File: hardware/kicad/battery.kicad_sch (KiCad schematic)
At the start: 4 parts, among them J2 +LIPO, J3 -LIPO, Q1 AO3407A

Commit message: clean-up
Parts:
- TP1: footprint TestPoint:TestPoint_Pad_D1.5mm -> TestPoint:TestPoint_Pad_D1.0mm
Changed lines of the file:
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@@
       (effects (font (size 1.27 1.27)))
     )
-    (property "Footprint" "TestPoint:TestPoint_Pad_D1.5mm" (at 111.76 52.07 0)
+    (property "Footprint" "TestPoint:TestPoint_Pad_D1.0mm" (at 111.76 52.07 0)
       (effects (font (size 1.27 1.27)) hide)
     )
@@
       (effects (font (size 1.27 1.27)) hide)
     )
+    (property "Part Description" "" (at 106.68 52.07 0)
+      (effects (font (size 1.27 1.27)) hide)
+    )
+    (property "Manufacturer" "" (at 106.68 52.07 0)
+      (effects (font (size 1.27 1.27)) hide)
+    )
+    (property "Manufacturer Part Number" "" (at 106.68 52.07 0)
+      (effects (font (size 1.27 1.27)) hide)
+    )
+    (property "Distributor" "" (at 106.68 52.07 0)
+      (effects (font (size 1.27 1.27)) hide)
+    )
+    (property "Distributor Part Number" "" (at 106.68 52.07 0)
+      (effects (font (size 1.27 1.27)) hide)
+    )
+    (property "Distributor Link" "" (at 106.68 52.07 0)
+      (effects (font (size 1.27 1.27)) hide)
+    )

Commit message: change batt footprint
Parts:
- J3: footprint TestPoint:TestPoint_Pad_2.0x2.0mm -> TestPoint:TestPoint_Loop_D1.80mm_Drill1.0mm_Beaded
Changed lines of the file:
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@@
       (effects (font (size 1.27 1.27)))
     )
-    (property "Footprint" "TestPoint:TestPoint_Pad_2.0x2.0mm" (at 101.6 64.77 0)
+    (property "Footprint" "TestPoint:TestPoint_Loop_D1.80mm_Drill1.0mm_Beaded" (at 101.6 64.77 0)
       (effects (font (size 1.27 1.27)) hide)
     )
@@
       (effects (font (size 1.27 1.27)) hide)
     )
+    (property "Manufacturer" "" (at 101.6 64.77 0)
+      (effects (font (size 1.27 1.27)) hide)
+    )
+    (property "Manufacturer Part Number" "" (at 101.6 64.77 0)
+      (effects (font (size 1.27 1.27)) hide)
+    )
+    (property "Distributor" "" (at 101.6 64.77 0)
+      (effects (font (size 1.27 1.27)) hide)
+    )
+    (property "Distributor Part Number" "" (at 101.6 64.77 0)
+      (effects (font (size 1.27 1.27)) hide)
+    )
+    (property "Distributor Link" "" (at 101.6 64.77 0)
+      (effects (font (size 1.27 1.27)) hide)
+    )

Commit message: change batt footprint
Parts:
- J2: footprint TestPoint:TestPoint_Pad_2.0x2.0mm -> TestPoint:TestPoint_THTPad_D1.0mm_Drill0.5mm
- J3: footprint TestPoint:TestPoint_Loop_D1.80mm_Drill1.0mm_Beaded -> TestPoint:TestPoint_THTPad_D1.0mm_Drill0.5mm
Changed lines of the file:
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@@
       (effects (font (size 1.27 1.27)))
     )
-    (property "Footprint" "TestPoint:TestPoint_Pad_2.0x2.0mm" (at 101.6 59.69 0)
+    (property "Footprint" "TestPoint:TestPoint_THTPad_D1.0mm_Drill0.5mm" (at 101.6 59.69 0)
       (effects (font (size 1.27 1.27)) hide)
     )
@@
     )
     (property "Part Description" "On-board Pad" (at 101.6 59.69 0)
+      (effects (font (size 1.27 1.27)) hide)
+    )
+    (property "Manufacturer" "" (at 101.6 59.69 0)
+      (effects (font (size 1.27 1.27)) hide)
+    )
+    (property "Manufacturer Part Number" "" (at 101.6 59.69 0)
+      (effects (font (size 1.27 1.27)) hide)
+    )
+    (property "Distributor" "" (at 101.6 59.69 0)
+      (effects (font (size 1.27 1.27)) hide)
+    )
+    (property "Distributor Part Number" "" (at 101.6 59.69 0)
+      (effects (font (size 1.27 1.27)) hide)
+    )
+    (property "Distributor Link" "" (at 101.6 59.69 0)
       (effects (font (size 1.27 1.27)) hide)
     )
@@
       (effects (font (size 1.27 1.27)))
     )
-    (property "Footprint" "TestPoint:TestPoint_Loop_D1.80mm_Drill1.0mm_Beaded" (at 101.6 64.77 0)
+    (property "Footprint" "TestPoint:TestPoint_THTPad_D1.0mm_Drill0.5mm" (at 101.6 64.77 0)
       (effects (font (size 1.27 1.27)) hide)
     )

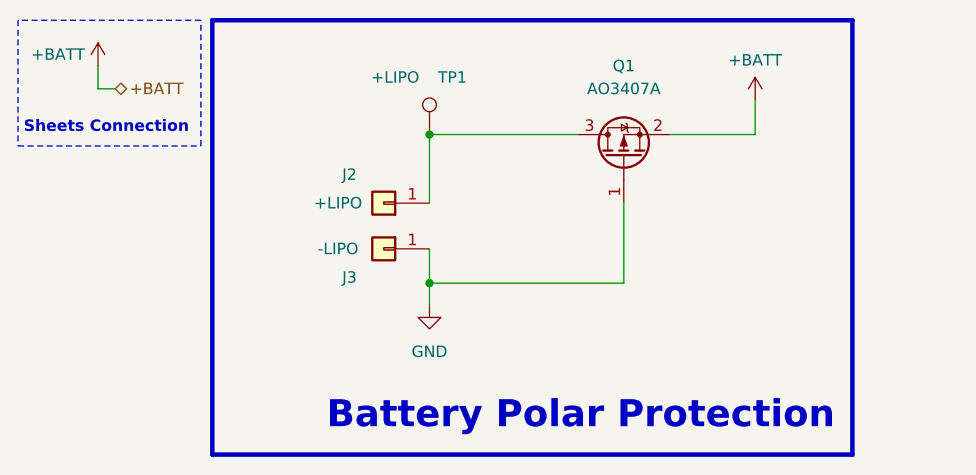
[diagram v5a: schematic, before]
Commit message: add jst battery
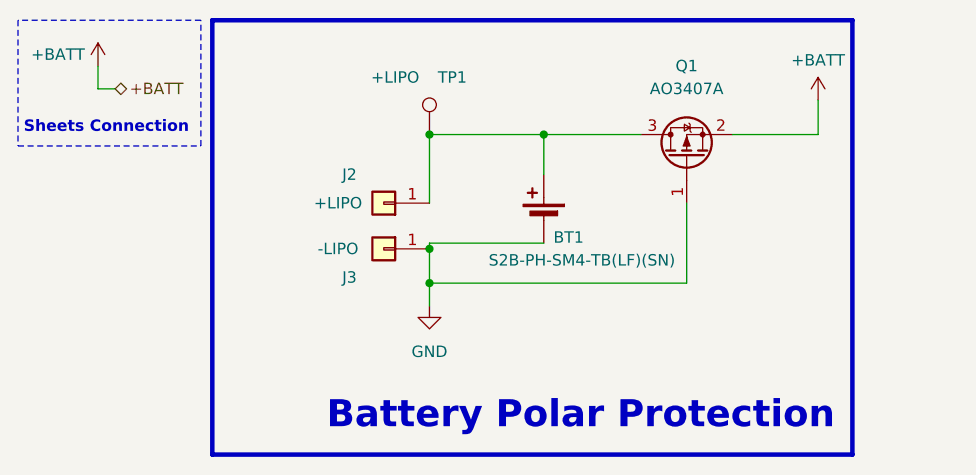
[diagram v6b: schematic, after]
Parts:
- added BT1: S2B-PH-SM4-TB(LF)(SN), plantpal:JST_PH_S2B-PH-SM4-TB_1x02-1MP_P2.00mm_Horizontal, symbol Device:Battery_Cell
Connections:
- net GND: now also BT1.2 (-)
- net at J2.1 (Pin_1), Q1.3 (D), TP1.1: now also BT1.1 (+)
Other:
- moved on the sheet: Q1
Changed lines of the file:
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@@
   (junction (at 106.68 52.07) (diameter 0) (color 0 0 0 0)
   )
+  (junction (at 119.38 52.07) (diameter 0) (color 0 0 0 0)
+  )
+  (junction (at 106.68 64.77) (diameter 0) (color 0 0 0 0)
+  )
   (junction (at 106.68 68.58) (diameter 0) (color 0 0 0 0)
   )
-  (wire (pts (xy 128.27 59.69) (xy 128.27 68.58))
+  (wire (pts (xy 135.255 59.69) (xy 135.255 68.58))
     (stroke (width 0) (type default))
   )
@@
     (stroke (width 0) (type dash))
   )
-  (wire (pts (xy 142.875 48.26) (xy 142.875 52.07))
+  (wire (pts (xy 106.68 68.58) (xy 106.68 71.12))
+    (stroke (width 0) (type default))
+  )
+  (wire (pts (xy 149.86 48.26) (xy 149.86 52.07))
     (stroke (width 0) (type default))
   )
@@
     (stroke (width 0) (type dash))
   )
+  (wire (pts (xy 119.38 52.07) (xy 130.175 52.07))
+    (stroke (width 0) (type default))
+  )
   (polyline (pts (xy 153.67 39.37) (xy 153.67 87.63))
     (stroke (width 0.5) (type default))
@@
     (stroke (width 0) (type default))
   )
-  (wire (pts (xy 133.35 52.07) (xy 142.875 52.07))
+  (wire (pts (xy 140.335 52.07) (xy 149.86 52.07))
     (stroke (width 0) (type default))
   )
@@
     (stroke (width 0.5) (type default))
   )
+  (wire (pts (xy 119.38 64.135) (xy 106.68 64.135))
+    (stroke (width 0) (type default))
+  )
   (polyline (pts (xy 81.28 53.34) (xy 81.28 39.37))
     (stroke (width 0) (type dash))
   )
-  (wire (pts (xy 106.68 68.58) (xy 106.68 71.12))
-    (stroke (width 0) (type default))
-  )
   (wire (pts (xy 106.68 64.77) (xy 106.68 68.58))
     (stroke (width 0) (type default))
   )
-  (wire (pts (xy 106.68 68.58) (xy 128.27 68.58))
+  (wire (pts (xy 119.38 52.07) (xy 119.38 56.515))
+    (stroke (width 0) (type default))
+  )
+  (wire (pts (xy 106.68 68.58) (xy 135.255 68.58))
     (stroke (width 0) (type default))
   )
@@
     (stroke (width 0.5) (type default))
   )
+  (wire (pts (xy 106.68 64.135) (xy 106.68 64.77))
+    (stroke (width 0) (type default))
+  )
   (wire (pts (xy 69.85 46.99) (xy 71.755 46.99))
     (stroke (width 0) (type default))
@@
     (stroke (width 0.5) (type default))
   )
-  (wire (pts (xy 106.68 52.07) (xy 123.19 52.07))
+  (wire (pts (xy 106.68 52.07) (xy 119.38 52.07))
     (stroke (width 0) (type default))
   )
@@
     (effects (font (size 1.27 1.27)) (justify left))
   )
-  (symbol (lib_id "Device:Q_PMOS_GSD") (at 128.27 54.61 90) (unit 1)
+  (symbol (lib_id "Device:Battery_Cell") (at 119.38 61.595 0) (mirror y) (unit 1)
+    (in_bom yes) (on_board yes) (dnp no)
+    (property "Reference" "BT1" (at 123.825 63.5 0)
+      (effects (font (size 1.27 1.27)) (justify left))
+    )
+    (property "Value" "S2B-PH-SM4-TB(LF)(SN)" (at 133.985 66.04 0)
+      (effects (font (size 1.27 1.27)) (justify left))
+    )
+    (property "Footprint" "plantpal:JST_PH_S2B-PH-SM4-TB_1x02-1MP_P2.00mm_Horizontal" (at 119.38 60.071 90)
+      (effects (font (size 1.27 1.27)) hide)
+    )
+    (property "Datasheet" "https://datasheet.lcsc.com/lcsc/2102031704_JST-Sales-America-S2B-PH-SM4-TB-LF-SN_C295747.pdf" (at 119.38 60.071 90)
+      (effects (font (size 1.27 1.27)) hide)
+    )
+    (property "Part Description" "Wire To Board Connector 1x2P PH 2mm Male 2A P=2mm" (at 119.38 61.595 0)
+      (effects (font (size 1.27 1.27)) hide)
+    )
+    (property "Manufacturer" "JST Sales America" (at 119.38 61.595 0)
+      (effects (font (size 1.27 1.27)) hide)
+    )
+    (property "Manufacturer Part Number" "S2B-PH-SM4-TB(LF)(SN)" (at 119.38 61.595 0)
+      (effects (font (size 1.27 1.27)) hide)
+    )
+    (property "Distributor" "LCSC" (at 119.38 61.595 0)
+      (effects (font (size 1.27 1.27)) hide)
+    )
+    (property "Distributor Part Number" "C295747" (at 119.38 61.595 0)
+      (effects (font (size 1.27 1.27)) hide)
+    )
+    (property "Distributor Link" "https://www.lcsc.com/product-detail/Wire-To-Board-Wire-To-Wire-Connector_JST-Sales-America-S2B-PH-SM4-TB-LF-SN_C295747.html" (at 119.38 61.595 0)
+      (effects (font (size 1.27 1.27)) hide)
+    )
+    (pin "1")
+    (pin "2")
+    (instances
+      (project "plantpal"
+        (path "/59b4123e-c7be-466b-a5db-658b8f0c1171/76cc1a03-b597-4ef0-85b8-85a2d617e76b"
+          (reference "BT1") (unit 1)
+        )
+      )
+    )
+  )
+  (symbol (lib_id "Device:Q_PMOS_GSD") (at 135.255 54.61 90) (unit 1)
     (in_bom yes) (on_board yes) (dnp no) (fields_autoplaced)
-    (property "Reference" "Q1" (at 128.27 44.45 90)
-      (effects (font (size 1.27 1.27)))
-    )
-    (property "Value" "AO3407A" (at 128.27 46.99 90)
-      (effects (font (size 1.27 1.27)))
-    )
-    (property "Footprint" "Package_TO_SOT_SMD:SOT-23" (at 125.73 49.53 0)
-      (effects (font (size 1.27 1.27)) hide)
-    )
-    (property "Datasheet" "https://datasheet.lcsc.com/lcsc/1810231523_Alpha---Omega-Semicon-AO3407A_C15155.pdf" (at 128.27 54.61 0)
-      (effects (font (size 1.27 1.27)) hide)
-    )
-    (property "Part Description" "MOSFET P Channel 30V 4.3A 48mΩ@10V,4.3A 1.4W" (at 128.27 54.61 0)
-      (effects (font (size 1.27 1.27)) hide)
-    )
-    (property "Manufacturer" "Alpha & Omega Semicon" (at 128.27 54.61 0)
-      (effects (font (size 1.27 1.27)) hide)
-    )
-    (property "Manufacturer Part Number" "AO3407A" (at 128.27 54.61 0)
-      (effects (font (size 1.27 1.27)) hide)
-    )
-    (property "Distributor" "LCSC" (at 128.27 54.61 0)
-      (effects (font (size 1.27 1.27)) hide)
-    )
-    (property "Distributor Part Number" "C15155" (at 128.27 54.61 0)
-      (effects (font (size 1.27 1.27)) hide)
-    )
-    (property "Distributor Link" "https://www.lcsc.com/product-detail/MOSFETs_Alpha-Omega-Semicon-AO3407A_C15155.html" (at 128.27 54.61 0)
+    (property "Reference" "Q1" (at 135.255 44.45 90)
+      (effects (font (size 1.27 1.27)))
+    )
+    (property "Value" "AO3407A" (at 135.255 46.99 90)
+      (effects (font (size 1.27 1.27)))
+    )
+    (property "Footprint" "Package_TO_SOT_SMD:SOT-23" (at 132.715 49.53 0)
+      (effects (font (size 1.27 1.27)) hide)
+    )
+    (property "Datasheet" "https://datasheet.lcsc.com/lcsc/1810231523_Alpha---Omega-Semicon-AO3407A_C15155.pdf" (at 135.255 54.61 0)
+      (effects (font (size 1.27 1.27)) hide)
+    )
+    (property "Part Description" "MOSFET P Channel 30V 4.3A 48mΩ@10V,4.3A 1.4W" (at 135.255 54.61 0)
+      (effects (font (size 1.27 1.27)) hide)
+    )
+    (property "Manufacturer" "Alpha & Omega Semicon" (at 135.255 54.61 0)
+      (effects (font (size 1.27 1.27)) hide)
+    )
+    (property "Manufacturer Part Number" "AO3407A" (at 135.255 54.61 0)
+      (effects (font (size 1.27 1.27)) hide)
+    )
+    (property "Distributor" "LCSC" (at 135.255 54.61 0)
+      (effects (font (size 1.27 1.27)) hide)
+    )
+    (property "Distributor Part Number" "C15155" (at 135.255 54.61 0)
+      (effects (font (size 1.27 1.27)) hide)
+    )
+    (property "Distributor Link" "https://www.lcsc.com/product-detail/MOSFETs_Alpha-Omega-Semicon-AO3407A_C15155.html" (at 135.255 54.61 0)
       (effects (font (size 1.27 1.27)) hide)
     )
@@
     )
   )
-  (symbol (lib_id "power:+BATT") (at 142.875 48.26 0) (unit 1)
+  (symbol (lib_id "power:+BATT") (at 149.86 48.26 0) (unit 1)
     (in_bom yes) (on_board yes) (dnp no)
-    (property "Reference" "#PWR070" (at 142.875 52.07 0)
-      (effects (font (size 1.27 1.27)) hide)
-    )
-    (property "Value" "+BATT" (at 142.875 43.815 0)
-      (effects (font (size 1.27 1.27)))
-    )
-    (property "Footprint" "" (at 142.875 48.26 0)
-      (effects (font (size 1.27 1.27)) hide)
-    )
-    (property "Datasheet" "" (at 142.875 48.26 0)
-      (effects (font (size 1.27 1.27)) hide)
-    )
+    (property "Reference" "#PWR070" (at 149.86 52.07 0)
+      (effects (font (size 1.27 1.27)) hide)
+    )
+    (property "Value" "+BATT" (at 149.86 43.815 0)
+      (effects (font (size 1.27 1.27)))
+    )
+    (property "Footprint" "" (at 149.86 48.26 0)
+      (effects (font (size 1.27 1.27)) hide)
+    )
+    (property "Datasheet" "" (at 149.86 48.26 0)
+      (effects (font (size 1.27 1.27)) hide)
+    )
